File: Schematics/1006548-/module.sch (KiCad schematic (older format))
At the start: 0 parts

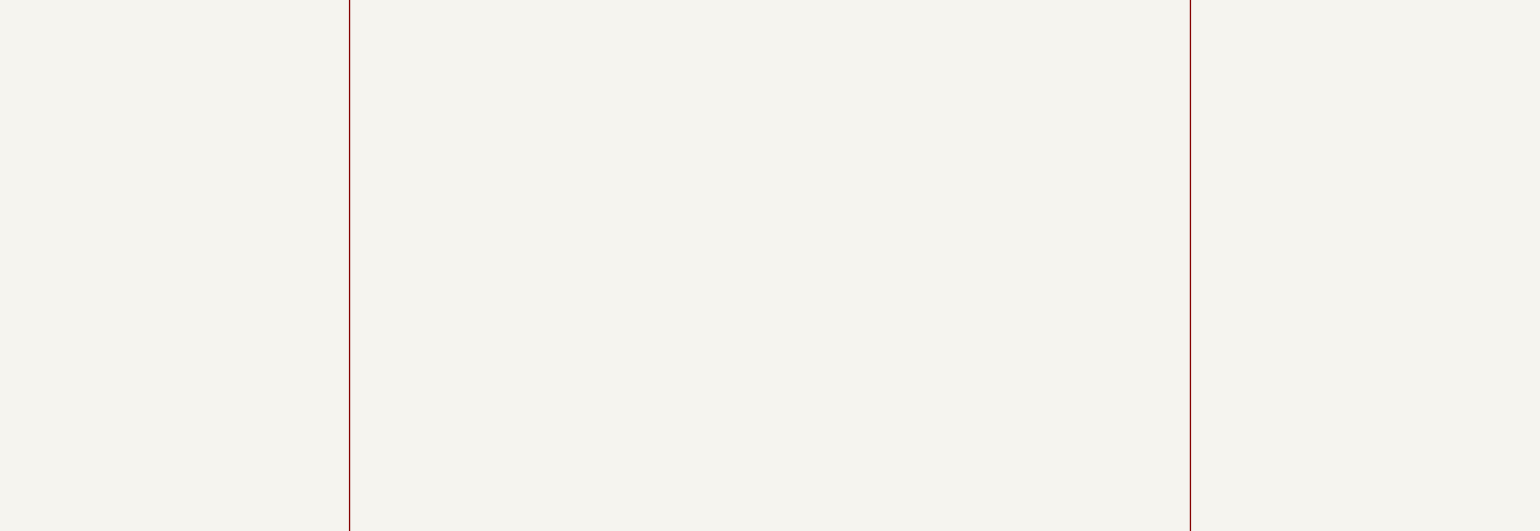
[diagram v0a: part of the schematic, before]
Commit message: Completed and proofed CAD transcription of drawing 1006548-.
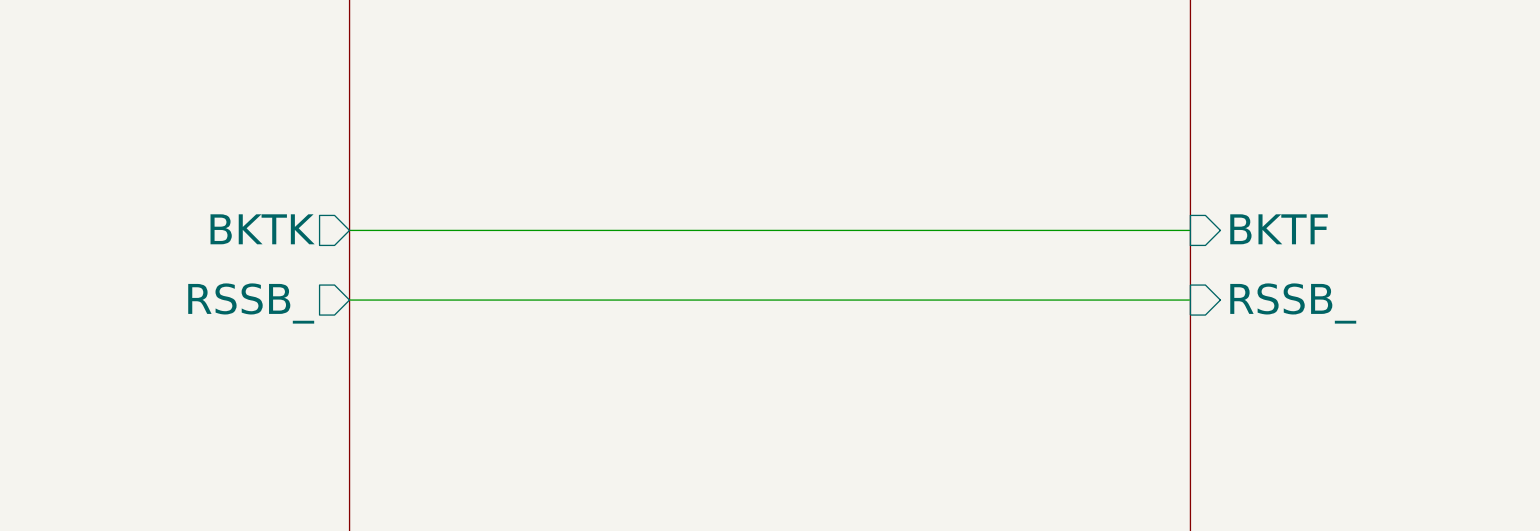
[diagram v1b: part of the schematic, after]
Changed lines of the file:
@@
 F2 "0VDC" U R 20150 16900 140
 F3 "+3VDC" U R 20150 15750 140
+F4 "BKTK" O R 20150 18125 140
+F5 "RSSB_" O R 20150 18450 140
 $EndSheet
 $Sheet
@@
 F2 "+3VDC" U L 24075 15750 140
 F3 "0VDC" U L 24075 16900 140
+F4 "BKTF" I L 24075 18125 140
+F5 "RSSB_" I L 24075 18450 140
 $EndSheet
 Text Notes 39300 31875 0    250  ~ 50
@@
 Wire Wire Line
 	24075 15750 20150 15750
+Wire Wire Line
+	20150 18125 24075 18125
+Wire Wire Line
+	24075 18450 20150 18450
 $EndSCHEMATC
